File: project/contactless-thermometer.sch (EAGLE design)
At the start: 92 parts, among them J1 OLED, J2 ICSP, J3 BLE, J4 USB-MINIB-5PIN, Q1 MMBT3904, Q2 MMBT3904, Q3 ZXMP6A17GTA, U1 LT1167CS8#PBF, U2 OPA2705UA, U3 OPA705NA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

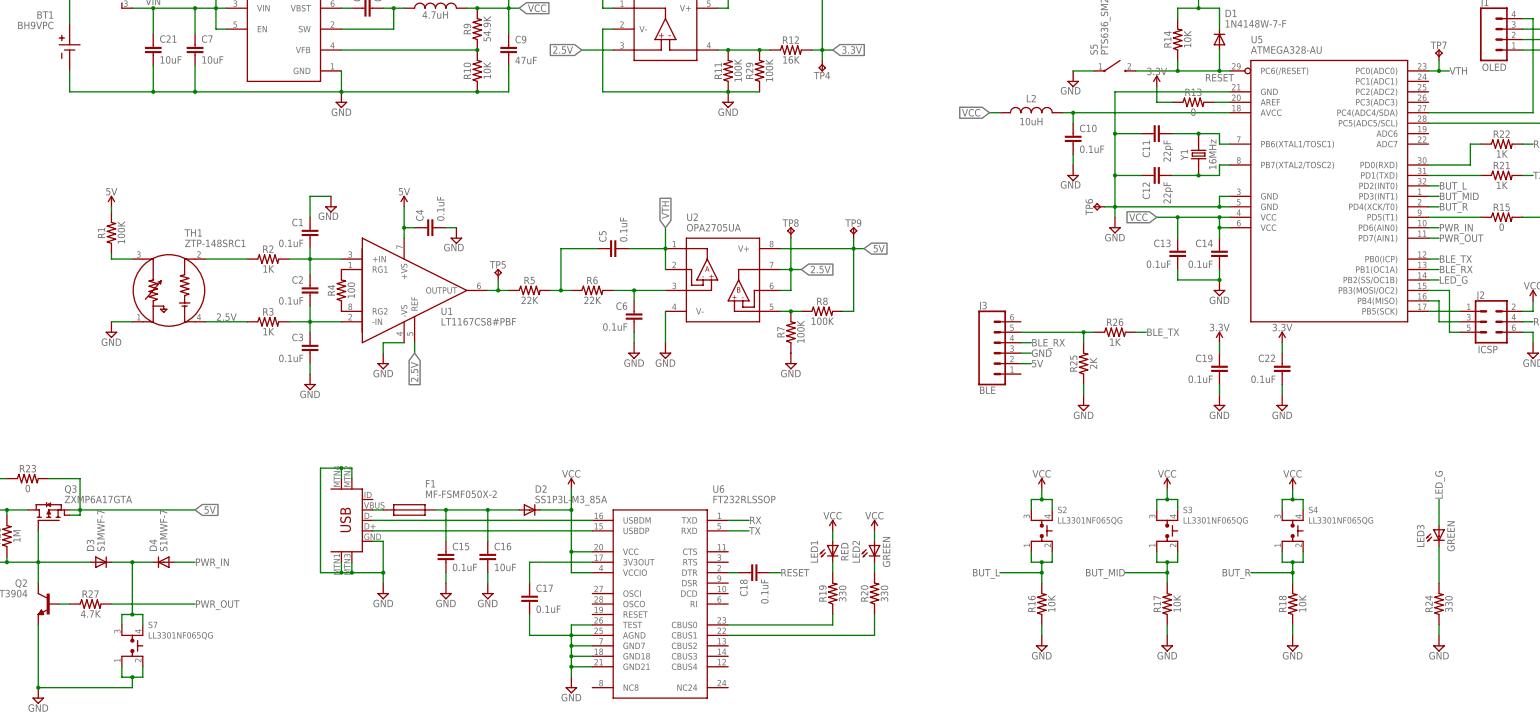
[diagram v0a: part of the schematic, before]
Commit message: update silkscreen and schematic
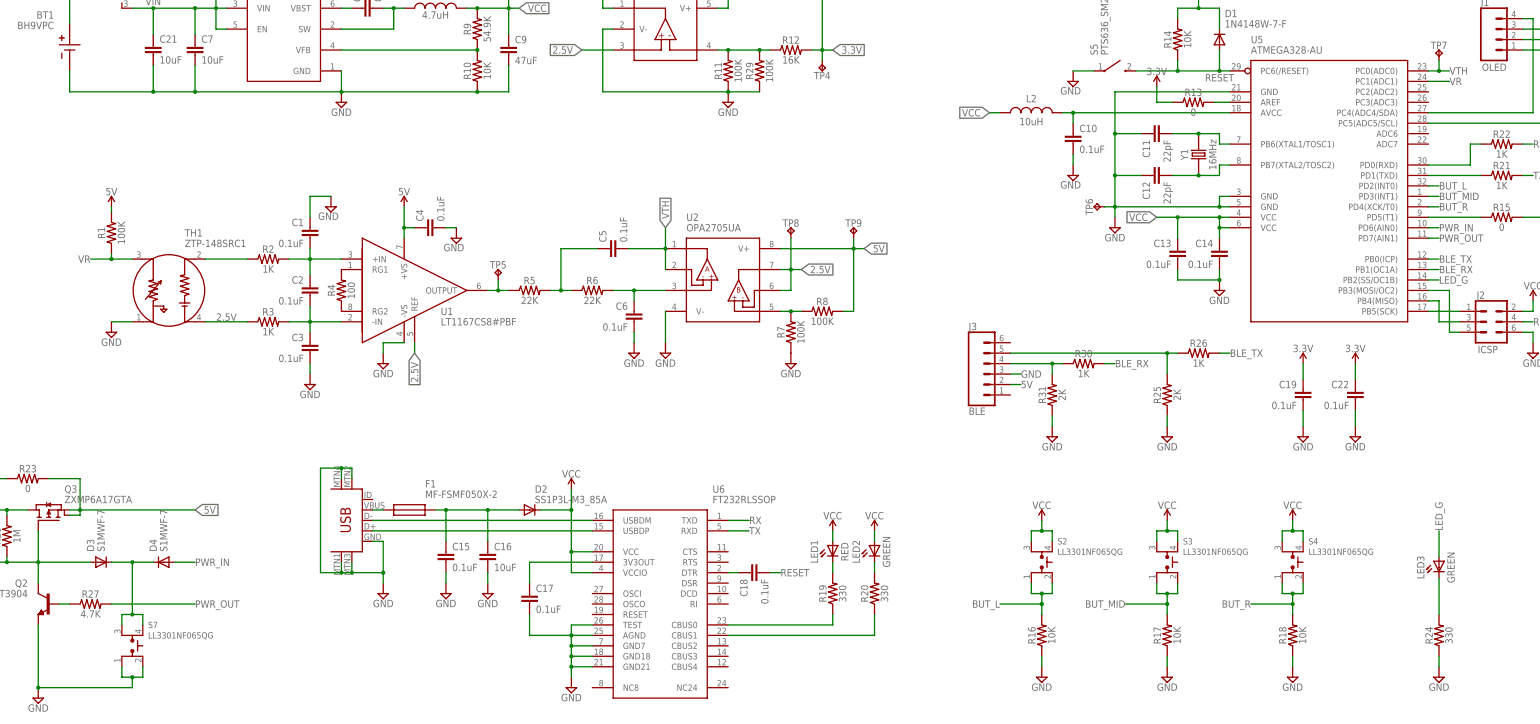
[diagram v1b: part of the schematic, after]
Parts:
- added R30: 1K, SparkFun-Resistors:RESISTOR0603
- added R31: 2K, SparkFun-Resistors:RESISTOR0603
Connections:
- removed net N$4: R1.1, TH1.THERMISTOR
- new net N$36: J3.4, R30.1, R31.2
- new net VR: R1.1, TH1.THERMISTOR, U5.PC1(ADC1)
- net BLE_RX: now also R30.2; no longer J3.4
- net GND: now also R31.1
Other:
- moved on the sheet: C19, C22, J3, LED3, R16, R17, R18, R24, R25, R26, S2, S3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
